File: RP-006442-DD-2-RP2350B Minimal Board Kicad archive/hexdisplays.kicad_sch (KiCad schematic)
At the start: 5 parts, among them U8 HT16K33A-24SSOP, U9 CC56-12EWA

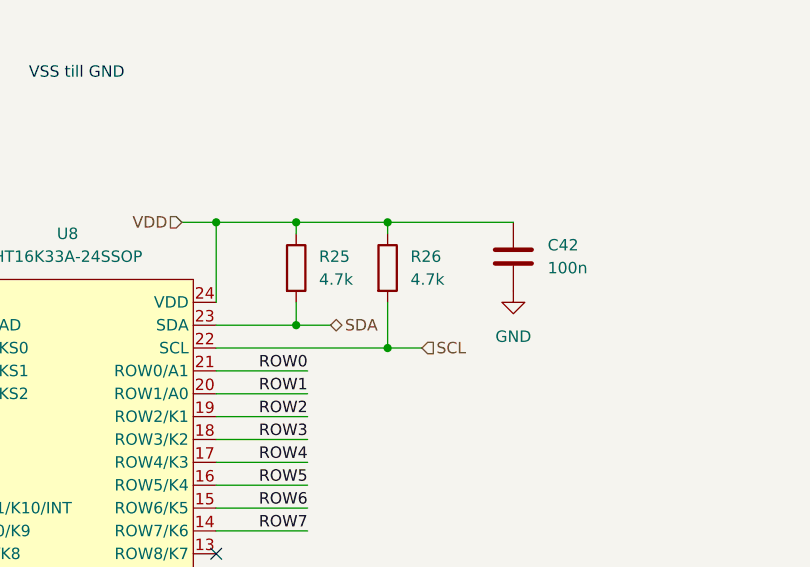
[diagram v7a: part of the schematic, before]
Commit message: Update accelerometer
Added accelerometer circuit to PCB editor
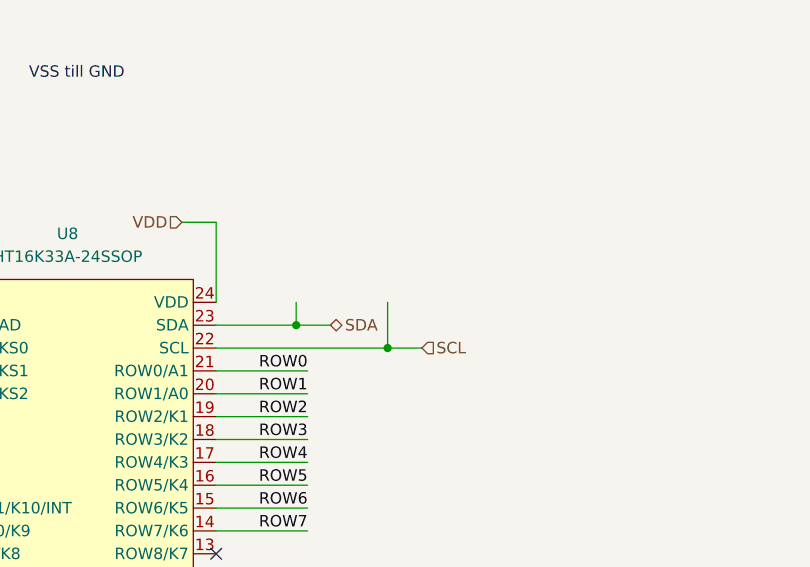
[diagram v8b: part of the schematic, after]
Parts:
- removed C42: 100n, Capacitor_SMD:C_0402_1005Metric, symbol Device:C
- removed R25, R26: 4.7k, Resistor_SMD:R_0402_1005Metric, symbol Device:R
